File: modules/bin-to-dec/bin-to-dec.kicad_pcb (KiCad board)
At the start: 4 copper layers, 36.1 x 48.9 mm, 78 parts, among them J1 Conn_02x26_Odd_Even, Q1 DMP3099L, Q10 2N7002, Q11 2N7002, Q12 DMP3099L, Q13 DMP3099L, Q14 2N7002, Q15 2N7002, Q16 2N7002, Q17 DMP3099L, Q18 DMP3099L, Q19 DMP3099L, Q2 DMP3099L, Q20 2N7002, Q21 2N7002, Q22 2N7002, Q23 DMP3099L, Q24 DMP3099L, Q25 DMP3099L, Q26 2N7002, Q27 2N7002, Q28 2N7002, Q29 DMP3099L, Q3 2N7002, Q30 DMP3099L, Q31 DMP3099L, Q32 2N7002, Q33 2N7002, Q34 DMP3099L, Q35 DMP3099L, Q36 2N7002, Q37 2N7002, Q38 2N7002, Q39 DMP3099L, Q4 2N7002, Q40 DMP3099L, Q41 DMP3099L, Q42 2N7002, Q43 2N7002, Q44 2N7002, Q45 DMP3099L, Q46 DMP3099L, Q47 DMP3099L, Q48 2N7002, Q49 2N7002, Q5 2N7002, Q50 2N7002, Q51 DMP3099L, Q52 DMP3099L, Q53 DMP3099L, Q54 2N7002, Q55 2N7002, Q56 2N7002, Q57 DMP3099L, Q58 DMP3099L, Q59 DMP3099L, Q6 2N7002, Q60 2N7002, Q61 2N7002, Q62 DMP3099L, Q63 DMP3099L, Q64 2N7002, Q65 2N7002, Q66 2N7002, Q67 DMP3099L, Q68 DMP3099L, Q69 DMP3099L, Q7 DMP3099L, Q70 2N7002, Q71 2N7002, Q72 2N7002, Q73 DMP3099L, Q74 DMP3099L, Q8 DMP3099L, Q9 DMP3099L

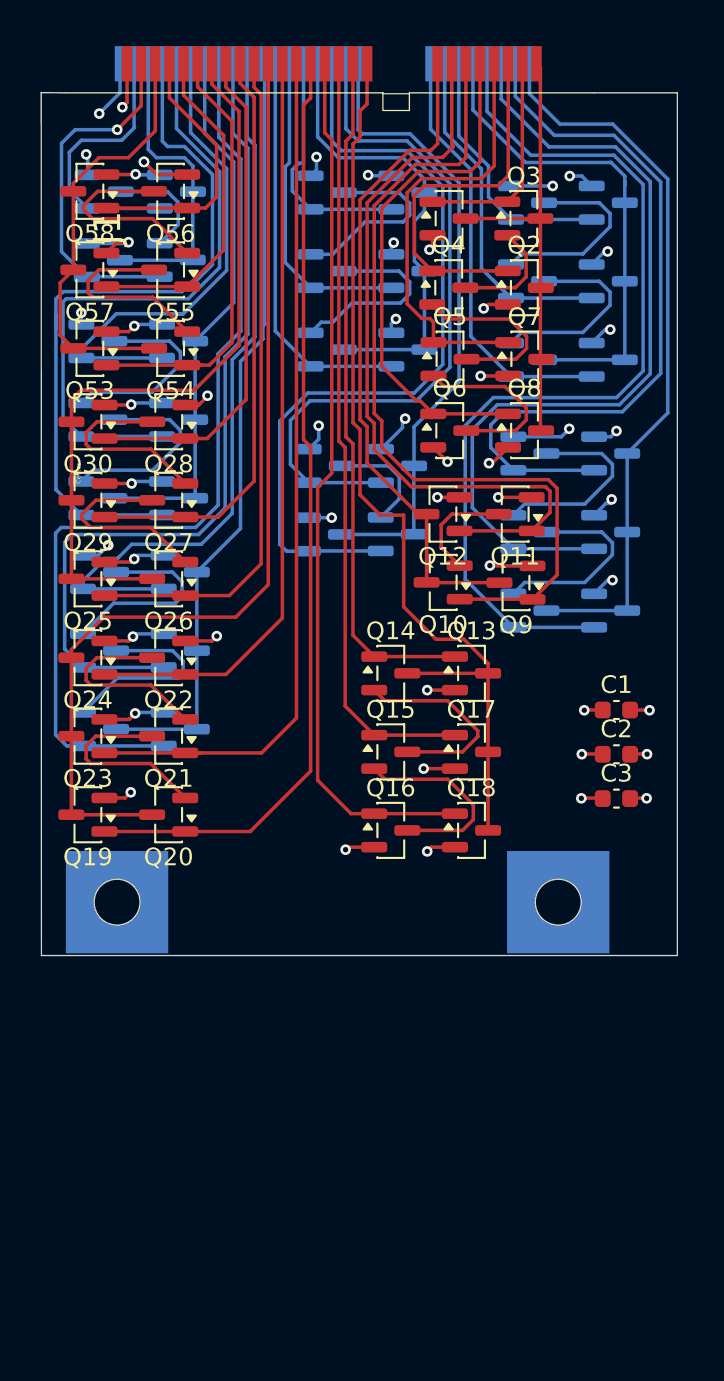
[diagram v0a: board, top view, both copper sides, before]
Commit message: move to correct dir. improved symmetry of pcb
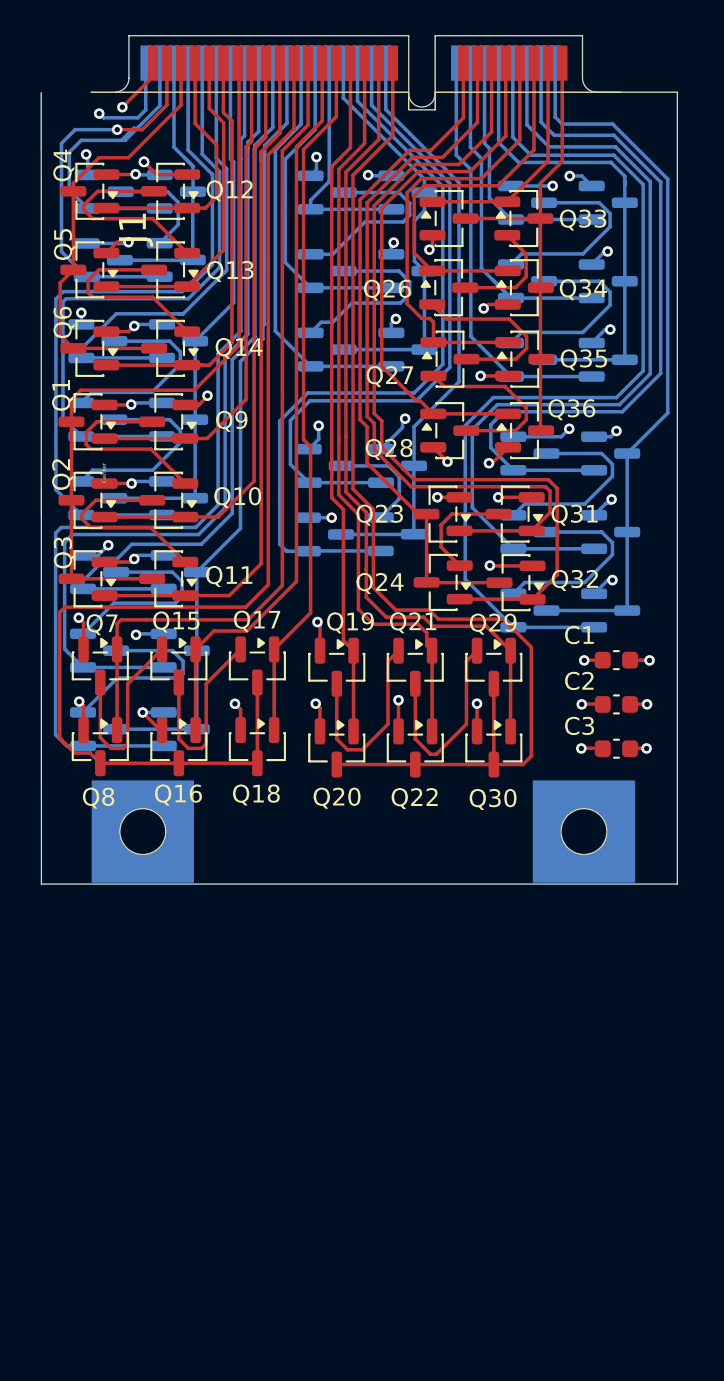
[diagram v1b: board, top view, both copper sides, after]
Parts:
- moved Q18 10.3 mm to (177.9, 120.2), turned to -90 degrees
- moved Q17 9.82 mm to (177.9, 115.6), turned to -90 degrees
- moved Q19 9.74 mm to (182.4, 115.7), turned to -90 degrees
- moved Q20 8.95 mm to (182.4, 120.3), turned to -90 degrees
- moved Q29 5.85 mm to (191.3, 115.7), turned to -90 degrees
- moved Q16 5.19 mm to (173.5, 120.2), turned to -90 degrees
- moved Q8 5.09 mm to (169.1, 120.2), turned to -90 degrees
- moved Q21 4.99 mm to (186.9, 115.7), turned to -90 degrees
- moved Q30 4.41 mm to (191.3, 120.3), turned to -90 degrees
- moved Q15 4.02 mm to (173.5, 115.6), turned to -90 degrees
- moved Q7 3.90 mm to (169.1, 115.6), turned to -90 degrees
- moved Q22 3.19 mm to (186.9, 120.3), turned to -90 degrees
- moved C1 2.83 mm to (198.3, 115.3)
- moved C2 2.83 mm to (198.3, 117.8)
- moved C3 2.82 mm to (198.3, 120.3)
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- renumbered Q30 to Q1, Q27 to Q10, Q26 to Q11, Q56 to Q12, Q55 to Q13, Q54 to Q14, Q21 to Q15, Q23 to Q16, Q20 to Q17, Q19 to Q18, Q16 to Q19, Q29 to Q2, Q18 to Q20, Q15 to Q21, Q17 to Q22, Q12 to Q23, Q10 to Q24, Q1 to Q25, Q4 to Q26, Q5 to Q27, Q6 to Q28, Q14 to Q29, Q25 to Q3, Q13 to Q30, Q11 to Q31, Q9 to Q32, Q3 to Q33, Q2 to Q34, Q7 to Q35, Q8 to Q36, Q68 to Q37, Q67 to Q38, Q63 to Q39, Q58 to Q4, Q74 to Q40, Q73 to Q41, Q69 to Q42, Q66 to Q43, Q65 to Q44, Q64 to Q45, Q72 to Q46, Q71 to Q47, Q70 to Q48, Q52 to Q49, Q57 to Q5, Q51 to Q50, Q47 to Q51, Q62 to Q52, Q60 to Q53, Q50 to Q54, Q49 to Q55, Q48 to Q56, Q61 to Q57, Q59 to Q58, Q46 to Q59, Q53 to Q6, Q45 to Q60, Q41 to Q61, Q40 to Q62, Q39 to Q63, Q35 to Q64, Q34 to Q65, Q32 to Q66, Q33 to Q67, Q31 to Q68, Q44 to Q69, Q22 to Q7, Q43 to Q70, Q42 to Q71, Q38 to Q72, Q37 to Q73, Q36 to Q74, Q24 to Q8, Q28 to Q9
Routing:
- net /nand3_2_A: track 53.6 -> 39.6 mm
- net /nand3_1_C: track 49.7 -> 38.8 mm
- net /nand3_1_out: track 53.2 -> 63.5 mm
- net /nand3_2_out: track 56.1 -> 66.1 mm
- net /nand3_2_B: track 49.7 -> 41.9 mm
- net /nand3_1_A: track 39.0 -> 45.6 mm
- net /nand3_2_C: track 42.8 -> 46.5 mm
- net /nand3_7_out: track 26.0 -> 23.2 mm
- net /nand2_3_A: track 45.3 -> 42.8 mm
- net /nand2_3_out: track 35.9 -> 33.6 mm
- net /nand2_3_B: track 39.6 -> 37.4 mm
- net /nand2_2_B: track 15.6 -> 17.3 mm
- net /nand2_2_A: track 20.1 -> 21.6 mm
- net +3V3: track 65.0 -> 66.3 mm, vias 33 -> 34
- net /nand3_1_B: track 43.5 -> 42.2 mm
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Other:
- board size 36.1 x 48.9 mm -> 36.1 x 48.1 mm

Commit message: using plugin to generate jlc production files
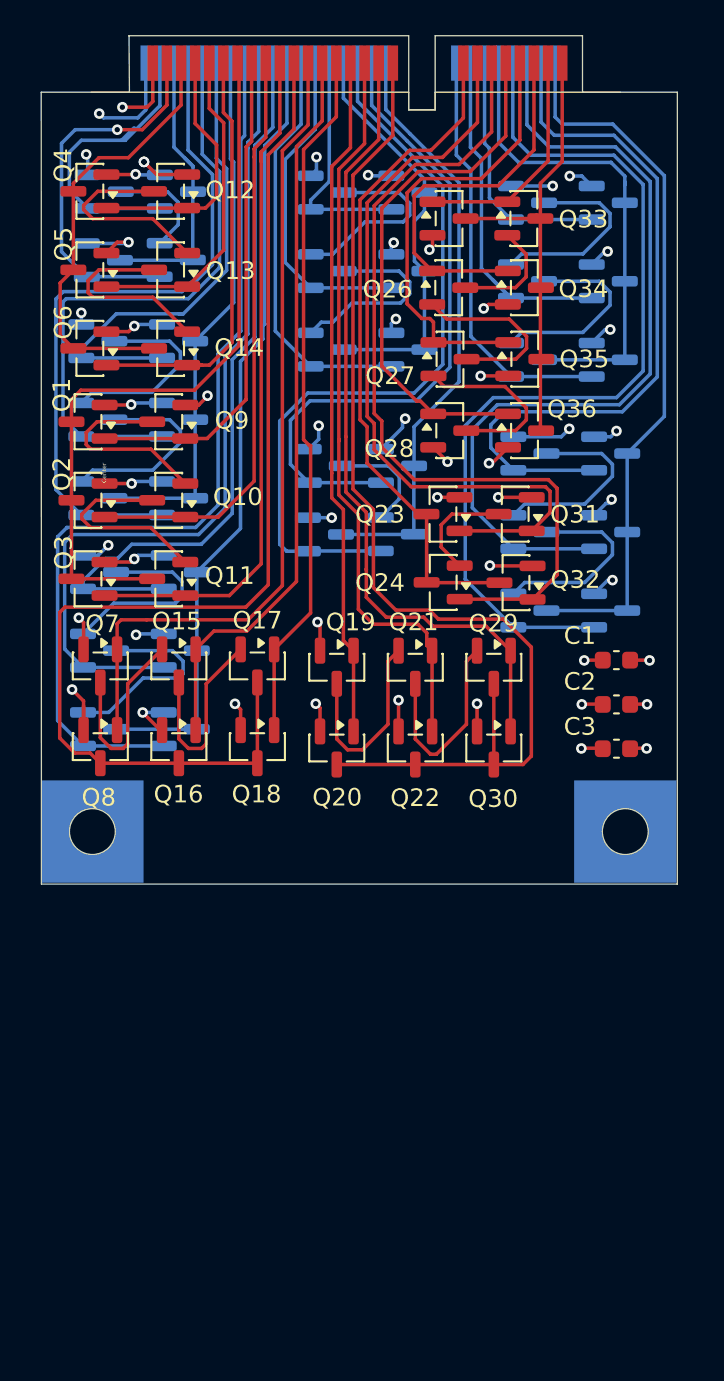
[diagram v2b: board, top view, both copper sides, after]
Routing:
- net +3V3: track 66.3 -> 68.5 mm
- net GND: track 29.9 -> 30.8 mm
- net /nand3_6_A: track 53.4 -> 52.5 mm
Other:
- outline, holes or cut-outs redrawn

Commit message: move components to top layer :(
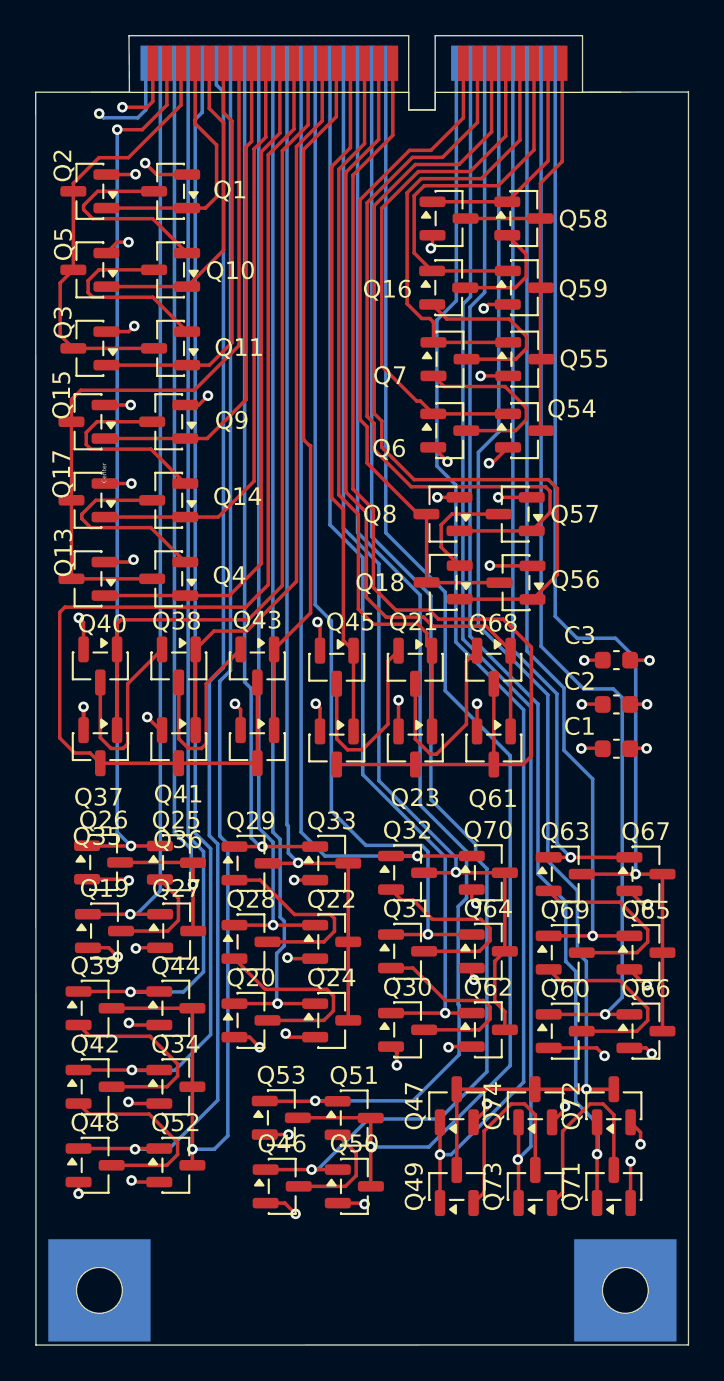
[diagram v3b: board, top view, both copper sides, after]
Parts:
- Q19: renamed from Q67; moved to F.Cu
- Q20: renamed from Q69; moved to F.Cu
- Q22: renamed from Q60; moved to F.Cu
- Q24: renamed from Q59; moved to F.Cu
- Q25: renamed from Q66; moved to F.Cu
- Q26: renamed from Q68; moved to F.Cu
- Q27: renamed from Q65; moved to F.Cu
- Q28: renamed from Q70; moved to F.Cu
- Q29: renamed from Q71; moved to F.Cu
- Q30: renamed from Q54; moved to F.Cu
- Q31: renamed from Q55; moved to F.Cu
- Q32: renamed from Q56; moved to F.Cu
- Q33: renamed from Q61; moved to F.Cu
- Q34: renamed from Q63; moved to F.Cu
- Q39: renamed from Q74; moved to F.Cu
- Q42: renamed from Q73; moved to F.Cu
- Q44: renamed from Q64; moved to F.Cu
- Q46: renamed from Q57; moved to F.Cu
- Q47: renamed from Q42; moved to F.Cu
- Q48: renamed from Q72; moved to F.Cu
- Q49: renamed from Q48; moved to F.Cu
- Q50: renamed from Q52; moved to F.Cu
- Q51: renamed from Q53; moved to F.Cu
- Q52: renamed from Q62; moved to F.Cu
- Q53: renamed from Q58; moved to F.Cu
- Q60: renamed from Q43; moved to F.Cu
- Q62: renamed from Q49; moved to F.Cu
- Q63: renamed from Q45; moved to F.Cu
- Q64: renamed from Q50; moved to F.Cu
- Q65: renamed from Q38; moved to F.Cu
- Q66: renamed from Q37; moved to F.Cu
- Q67: renamed from Q39; moved to F.Cu
- Q69: renamed from Q44; moved to F.Cu
- Q70: renamed from Q51; moved to F.Cu
- Q71: renamed from Q46; moved to F.Cu
- Q72: renamed from Q40; moved to F.Cu
- Q73: renamed from Q47; moved to F.Cu
- Q74: renamed from Q41; moved to F.Cu
- moved Q71 56.0 mm to (198.2, 145.1), turned to 90 degrees
- moved Q73 51.3 mm to (193.7, 145.1), turned to 90 degrees
- moved Q72 51.2 mm to (198.2, 140.5), turned to 90 degrees
- moved Q30 47.7 mm to (186.5, 136.2)
- moved Q62 47.7 mm to (191.0, 136.2)
- moved Q49 47.0 mm to (189.2, 145.1), turned to 90 degrees
- moved Q74 46.9 mm to (193.7, 140.5), turned to 90 degrees
- moved Q48 46.7 mm to (168.8, 143.9)
- moved Q52 46.7 mm to (173.3, 143.9)
- moved Q47 43.1 mm to (189.2, 140.5), turned to 90 degrees
- moved Q19 41.9 mm to (169.3, 130.6)
- moved Q27 41.9 mm to (173.4, 130.6)
- moved Q46 40.9 mm to (179.4, 145.1)
- moved Q50 40.9 mm to (183.4, 145.1)
- moved Q31 38.8 mm to (186.5, 131.8)
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- renumbered C3 to C1, C1 to C3, Q12 to Q1, Q13 to Q10, Q14 to Q11, Q25 to Q12, Q3 to Q13, Q10 to Q14, Q1 to Q15, Q26 to Q16, Q2 to Q17, Q24 to Q18, Q4 to Q2, Q22 to Q23, Q6 to Q3, Q18 to Q35, Q20 to Q36, Q8 to Q37, Q15 to Q38, Q11 to Q4, Q7 to Q40, Q16 to Q41, Q17 to Q43, Q19 to Q45, Q36 to Q54, Q35 to Q55, Q32 to Q56, Q31 to Q57, Q33 to Q58, Q34 to Q59, Q28 to Q6, Q30 to Q61, Q29 to Q68, Q27 to Q7, Q23 to Q8
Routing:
- net /nand3_8_C: track 14.1 -> 69.8 mm, vias 0 -> 1
- net /nand3_8_B: track 20.3 -> 68.8 mm, vias 0 -> 1
- net /nand3_7_C: track 13.3 -> 61.1 mm, vias 0 -> 1
- net /nand3_8_A: track 23.6 -> 71.3 mm, vias 0 -> 1
- net /nand3_8_out: track 27.6 -> 74.6 mm, vias 0 -> 1
- net /nand3_5_out: track 30.2 -> 77.0 mm, vias 0 -> 1
- net /nand2_3_out: track 33.6 -> 77.6 mm, vias 0 -> 1
- net /nand3_5_C: track 27.4 -> 69.9 mm, vias 0 -> 1
- net /nand3_7_B: track 18.6 -> 58.4 mm, vias 0 -> 1
- net /nand3_7_out: track 23.2 -> 62.4 mm, vias 0 -> 1
- net /nand2_3_B: track 37.4 -> 76.2 mm, vias 0 -> 1
- net /nand2_2_out: track 16.4 -> 55.0 mm, vias 0 -> 1
- net /nand2_2_B: track 17.3 -> 53.3 mm, vias 0 -> 1
- net /nand3_7_A: track 23.2 -> 55.3 mm, vias 0 -> 1
- net /nand3_5_B: track 34.3 -> 65.4 mm, vias 0 -> 1
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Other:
- board size 36.1 x 48.1 mm -> 37 x 74.2 mm

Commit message: switched to jlc basic components
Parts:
- Q12, Q13, Q15, Q17, Q2, Q22, Q23, Q24, Q26, Q27, Q3, Q33, Q34, Q35, Q36, Q37, Q41, Q44, Q47, Q5, Q50, Q52, Q53, Q54, Q55, Q56, Q59, Q61, Q62, Q64, Q65, Q66, Q67, Q70, Q72, Q74, Q8: value DMP3099L -> AO3401A

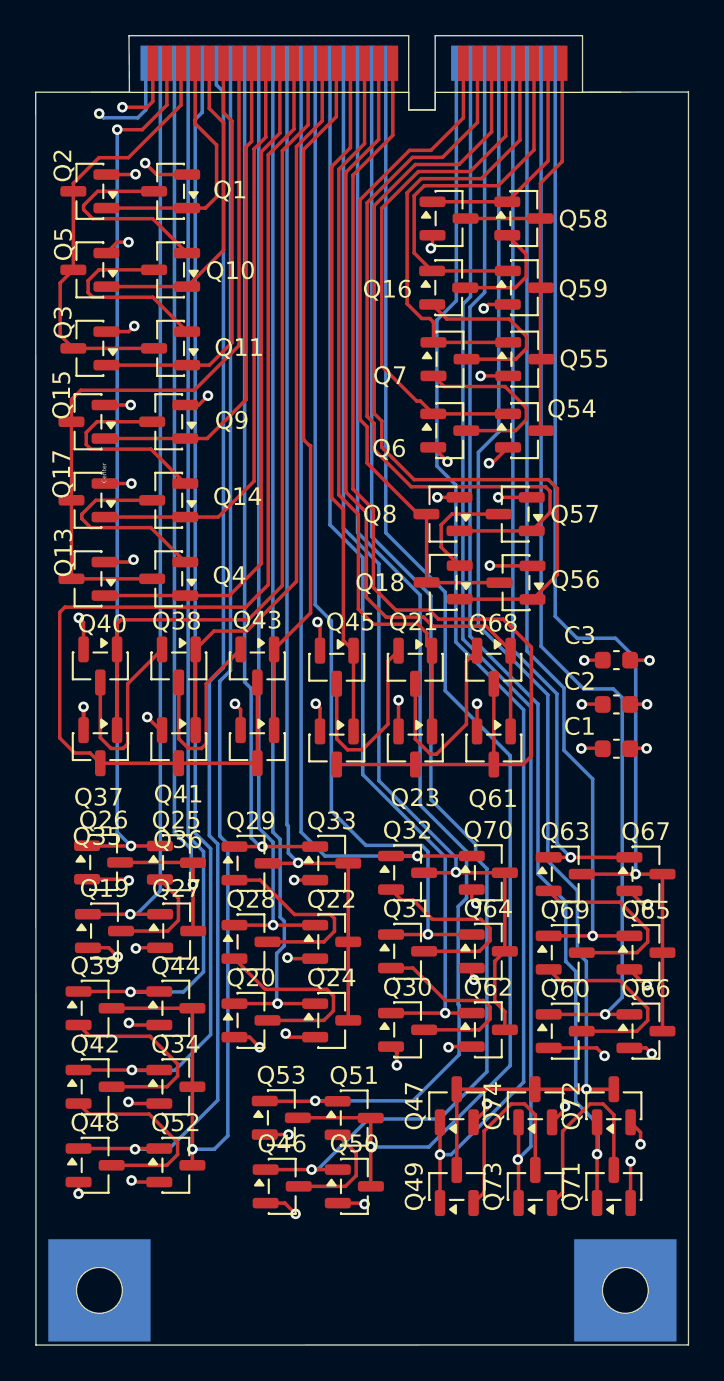
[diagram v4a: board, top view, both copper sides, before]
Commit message: moved designators
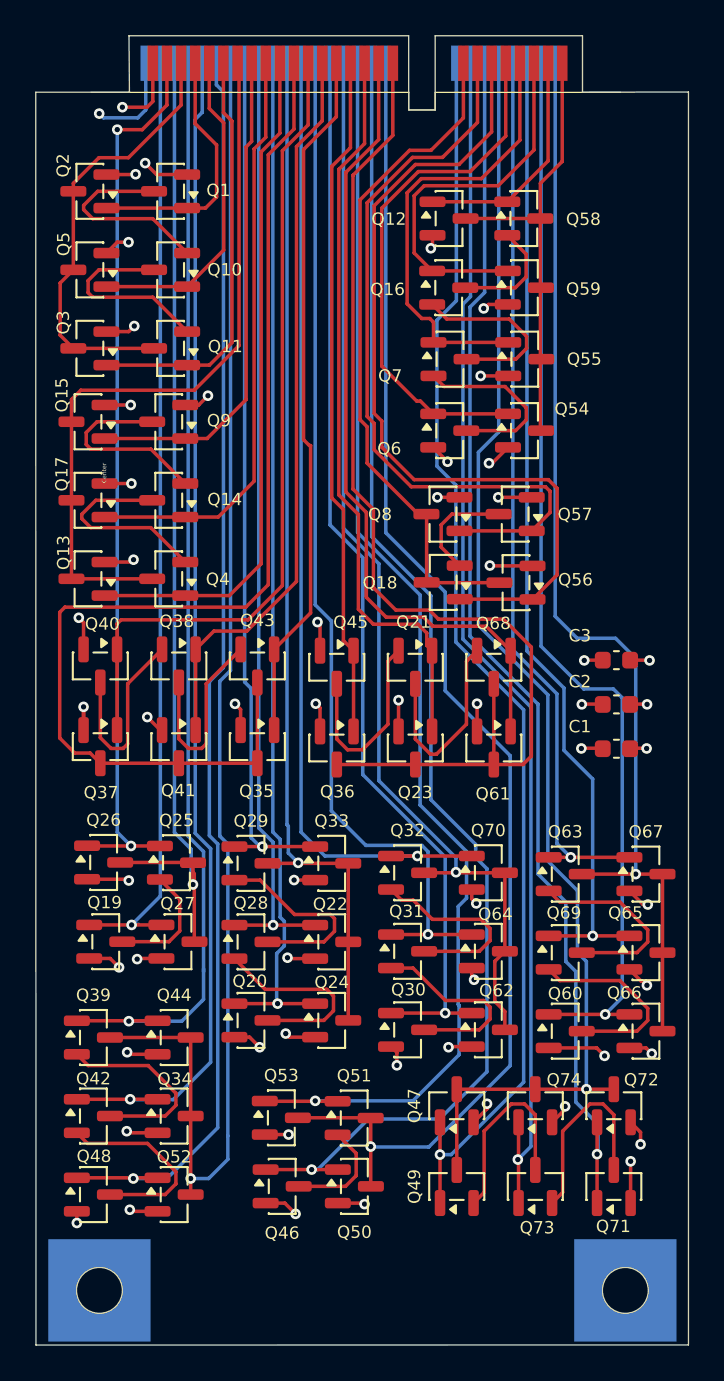
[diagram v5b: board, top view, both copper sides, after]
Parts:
- moved Q34 1.66 mm to (173.2, 141.1)
- moved Q42 1.66 mm to (168.7, 141.1)
- moved Q39 1.66 mm to (168.7, 136.7)
- moved Q44 1.66 mm to (173.2, 136.7)
- moved Q48 1.66 mm to (168.7, 145.6)
- moved Q52 1.66 mm to (173.2, 145.6)
- moved Q19 0.61 mm to (169.4, 131.2)
- moved Q27 0.61 mm to (173.4, 131.2)
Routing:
- net /nand3_5_A: track 61.0 -> 62.9 mm
- net /nand3_5_B: track 65.4 -> 67.1 mm
- net /nand3_5_C: track 69.9 -> 71.6 mm
- net /nand3_5_out: track 77.0 -> 78.6 mm
- net /nand2_2_out: track 55.0 -> 56.2 mm
- net /nand2_2_B: track 53.3 -> 54.1 mm
- net Net-(Q19-D): track 6.25 -> 6.89 mm

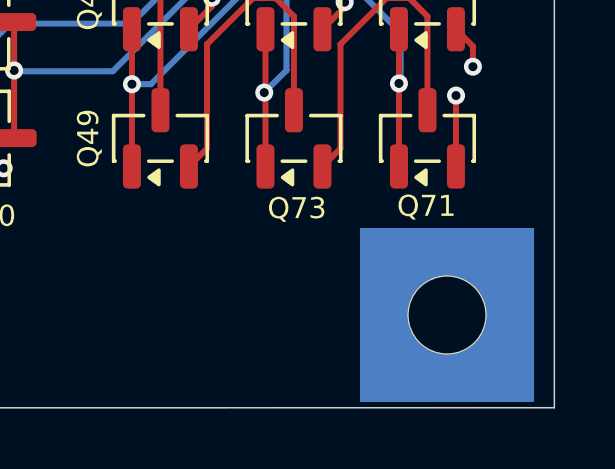
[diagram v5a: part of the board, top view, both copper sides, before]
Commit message: added footprints for modules
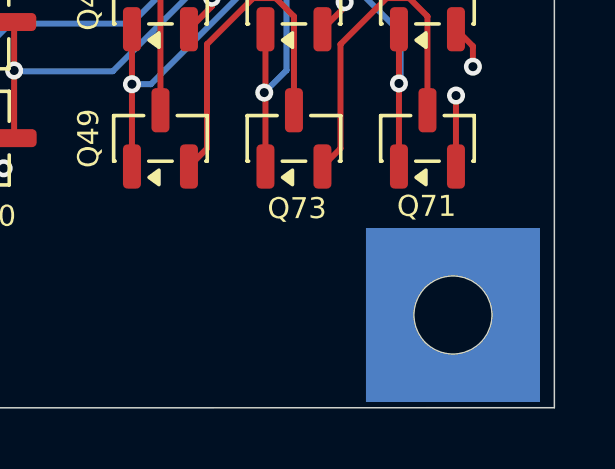
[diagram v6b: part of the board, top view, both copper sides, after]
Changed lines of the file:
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@@
 		)
 		(pad "" np_thru_hole circle
-			(at -15.275 -71.0922 180)
+			(at -15.4722 -71.0922 180)
 			(size 2.6 2.6)
 			(drill 2.6)
@@
 		)
 		(pad "" connect rect
-			(at -15.275 -71.0922 180)
+			(at -15.4722 -71.0922 180)
 			(size 5.8 5.8)
 			(layers "B.Cu" "B.SilkS")
